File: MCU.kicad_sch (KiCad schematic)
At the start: 82 parts, among them J401 EXPANSION, J402 RS485_1, J403 RS485_2, J404 Conn_ARM_JTAG_SWD_10, Q401 BC807, Q402 BC807, Q403 BC807, Q404 BC807, Q405 BC807, Q406 BC807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

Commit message: Synchronised PCB and schematic.
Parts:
- J404: footprint Connector_PinHeader_1.27mm:PinHeader_2x05_P1.27mm_Vertical_SMD -> petr:ArmHeader_2x05-1_P1.27mm_Vertical_SMD_pin7removed
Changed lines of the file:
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@@
       (effects (font (size 1.27 1.27)) (justify right))
     )
-    (property "Footprint" "Connector_PinHeader_1.27mm:PinHeader_2x05_P1.27mm_Vertical_SMD" (id 2) (at 271.78 140.97 0)
+    (property "Footprint" "petr:ArmHeader_2x05-1_P1.27mm_Vertical_SMD_pin7removed" (id 2) (at 271.78 140.97 0)
       (effects (font (size 1.27 1.27)) hide)
     )

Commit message: Some minor fixes
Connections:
- net VCC_AUX is gone; now on net VCC_MCU: C403.1
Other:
- moved on the sheet: C404, Q401, Q402, Q403, Q404, Q405, Q406, R410, R411, R412, R413, R414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

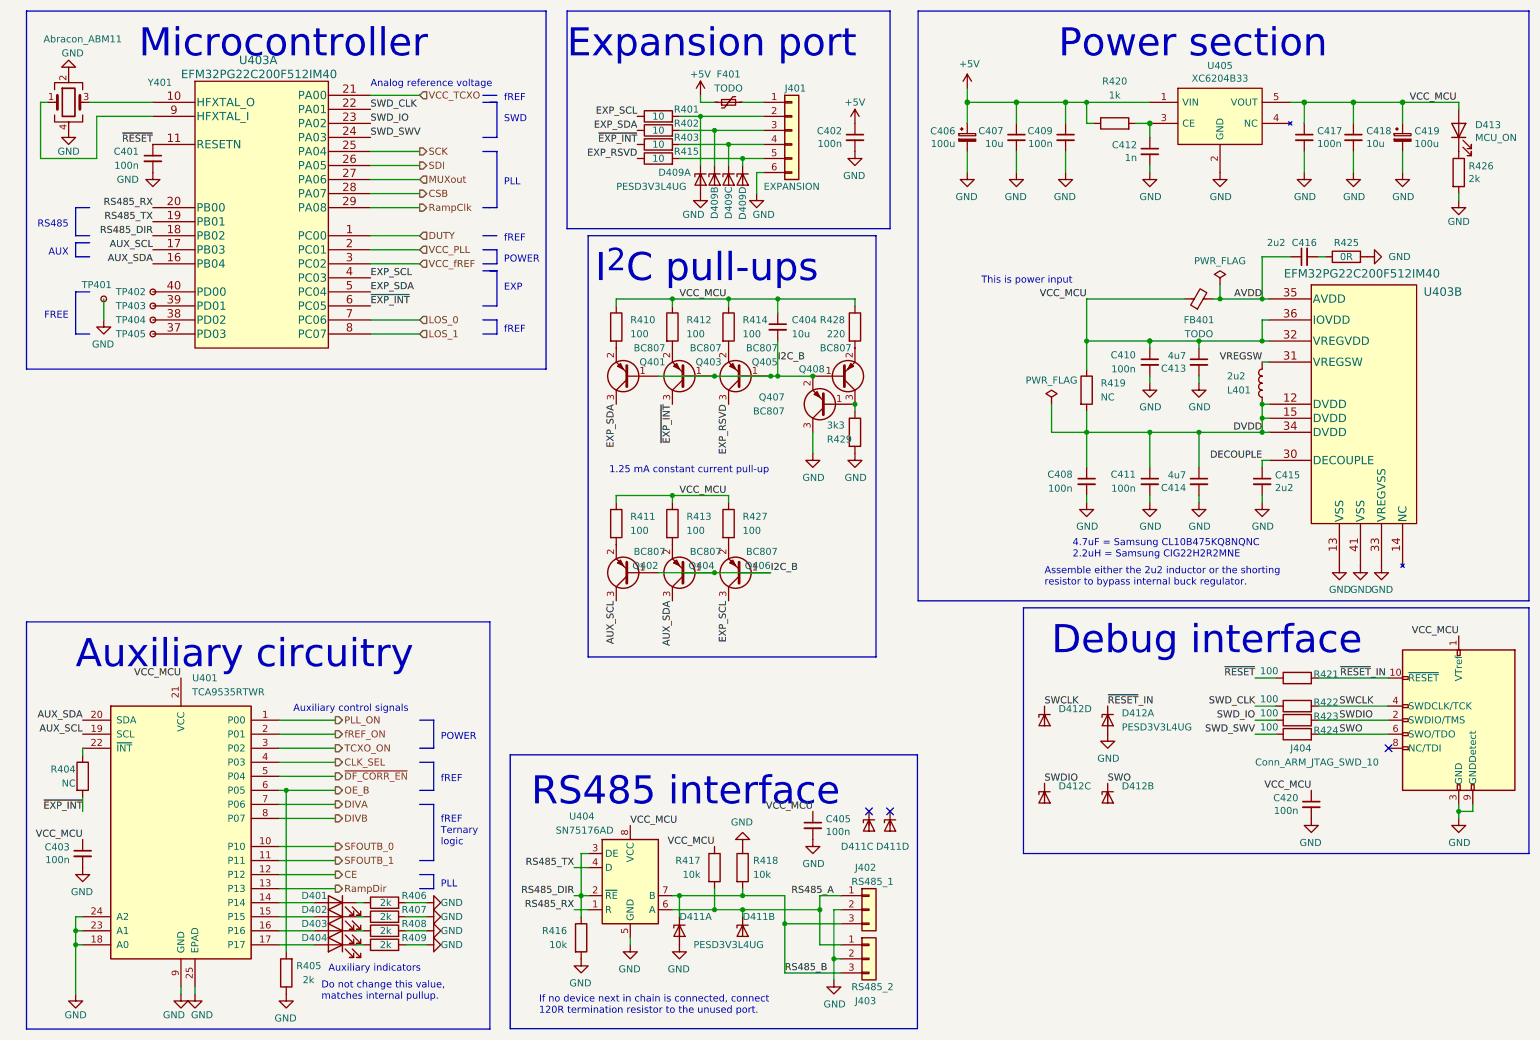
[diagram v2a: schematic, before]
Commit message: Minor improvements and fixes to schematic, added high current LDO needed for high frequency PLLs.
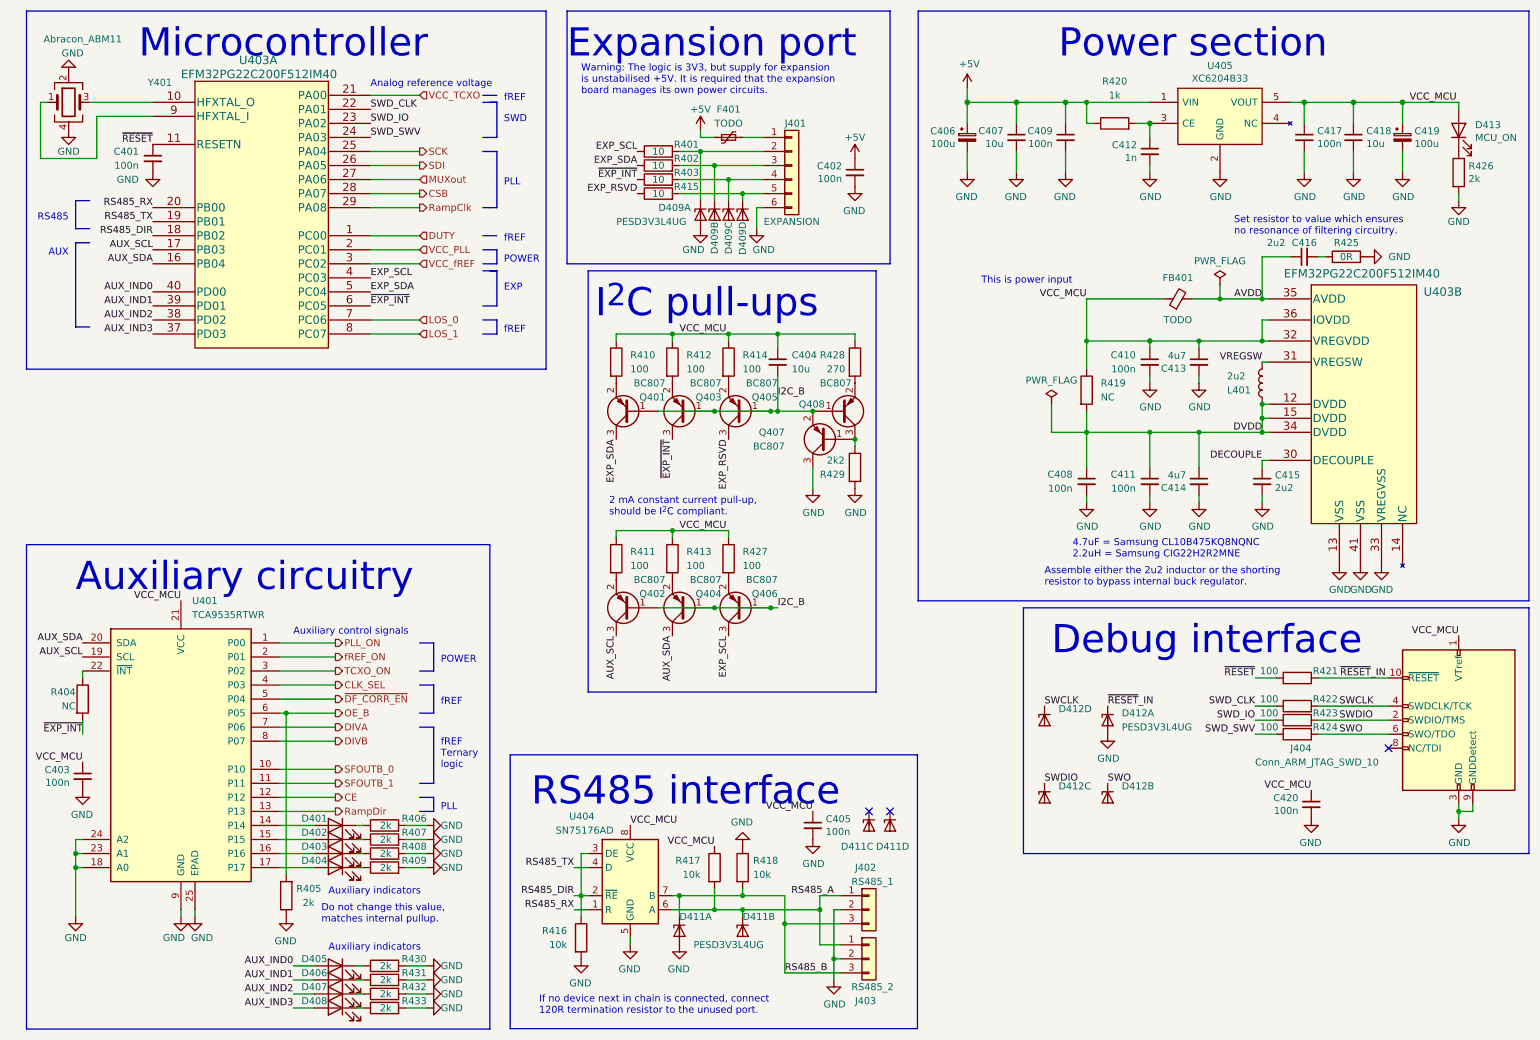
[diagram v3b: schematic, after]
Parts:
- removed TP401, TP402, TP403, TP404, TP405: TestPoint_Small, TestPoint:TestPoint_Pad_D1.0mm, symbol 4ms_Connector:TestPoint_Small
- added D405, D406, D407, D408: (no value), LED_SMD:LED_0603_1608Metric_Pad1.05x0.95mm_HandSolder, symbol Device:LED
- added R430, R431, R432, R433: 2k, Resistor_SMD:R_0603_1608Metric_Pad0.98x0.95mm_HandSolder, symbol Device:R
- R428: value 220 -> 270
- R429: value 3k3 -> 2k2
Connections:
- net GND: now also R430.2, R431.2, R432.2, R433.2
- net AUX_IND3: now reaches U403.37 (PD03)
- net AUX_IND3: now also D408.2 (A)
- net AUX_IND1: now reaches U403.39 (PD01)
- net AUX_IND1: now also D406.2 (A)
- net AUX_IND2: now reaches U403.38 (PD02)
- net AUX_IND2: now also D407.2 (A)
- net AUX_IND0: now reaches U403.40 (PD00)
- net AUX_IND0: now also D405.2 (A)
- new net: D406.1 (K), R431.1
- new net: D408.1 (K), R433.1
- new net: D405.1 (K), R430.1
- new net: D407.1 (K), R432.1
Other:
- note added: "2 mA constant current pull-up, should be I^{2}C compliant."
- note added: "Set resistor to value which ensures no resonance of filtering circuitry."
- note added: "Warning: The logic is 3V3, but supply for expansion is unstabilised +5V. It is required that the expansion board manages its own power circuits."
- note removed: "1.25 mA constant current pull-up"
- note removed: "FREE"
- moved on the sheet: C402, C403, C404, D401, D402, D403, D404, D409A, D409B, D409C, D409D, F401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
